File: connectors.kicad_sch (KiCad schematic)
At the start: 3 parts, among them X501 PH-00650, X502 S4B-PH-SM4-K-TB(LF)(SN), X503 USB3.1C16PFSMT

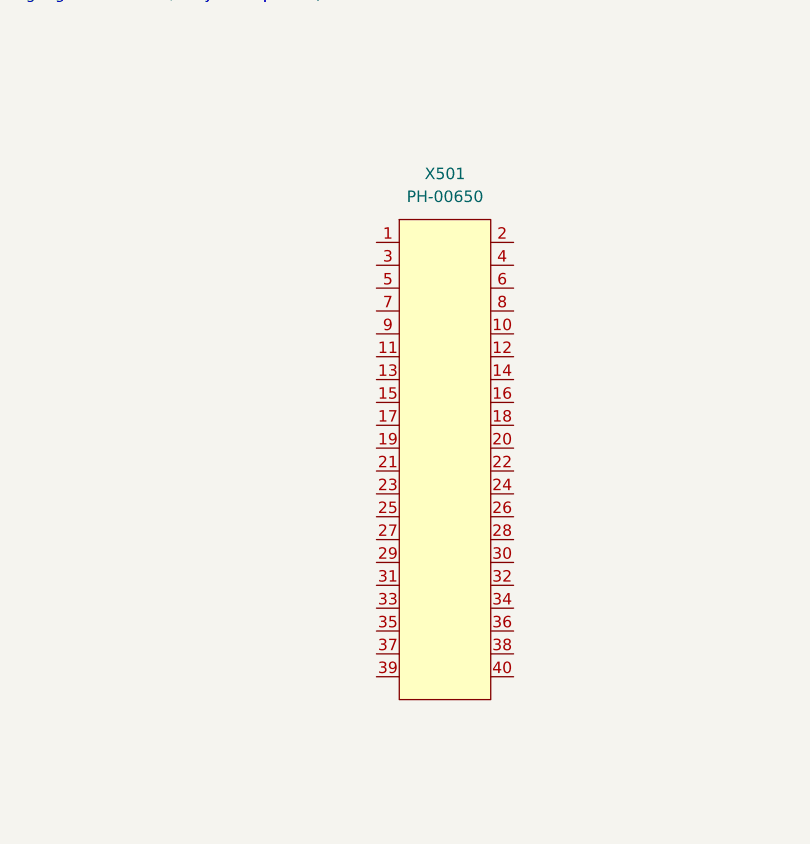
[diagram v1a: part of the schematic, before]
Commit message: Rough pcb placement for space estimation. Exchanged 40P connector
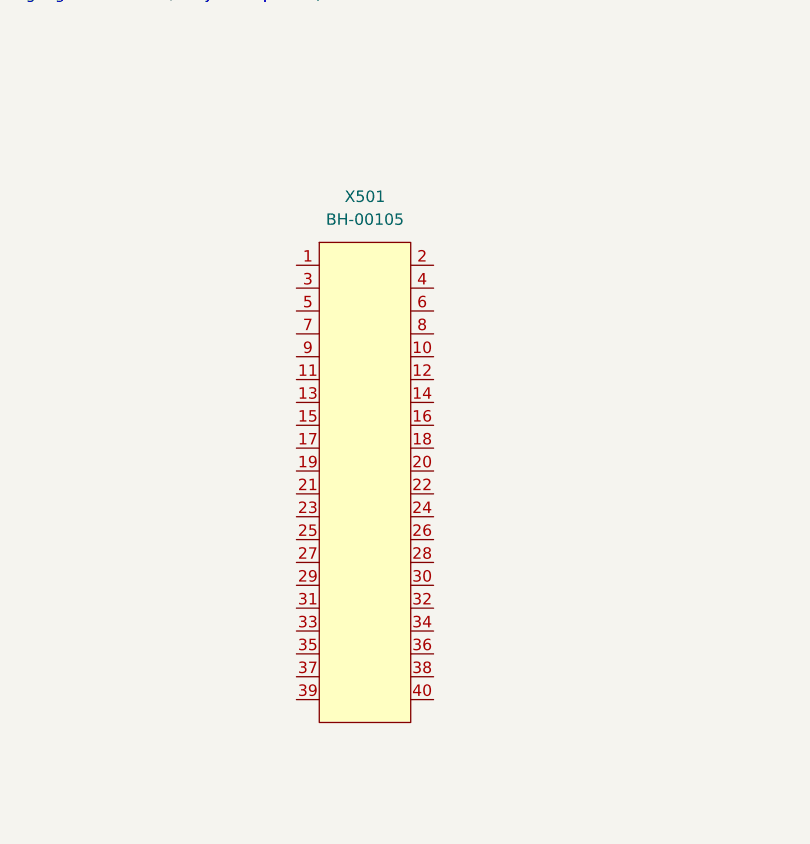
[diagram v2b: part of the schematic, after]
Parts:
- removed X501: PH-00650, HDR-SMD_40P-P2.54-V-M-R2-C20-S7.8-EH, symbol eduboardv2:PH-00650
- added X501: BH-00105, IDC-SMD_BH-00105, symbol eduboardv2:BH-00105
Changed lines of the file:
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@@
     (pin "1")
   )
-  (symbol (lib_id "eduboardv2:PH-00650") (at 78.74 81.28 0) (unit 1)
+  (symbol (lib_id "eduboardv2:GND") (at 175.26 110.49 0) (unit 1)
     (in_bom yes) (on_board yes) (fields_autoplaced)
-    (property "Reference" "X501" (id 0) (at 78.74 49.53 0))
-    (property "Value" "PH-00650" (id 1) (at 78.74 52.07 0))
-    (property "Footprint" "HDR-SMD_40P-P2.54-V-M-R2-C20-S7.8-EH" (id 2) (at 78.74 113.03 0)
+    (property "Reference" "#PWR0504" (id 0) (at 175.26 116.84 0)
       (effects (font (size 1.27 1.27)) hide)
     )
-    (property "Datasheet" "" (id 3) (at 78.74 81.28 0)
+    (property "Value" "GND" (id 1) (at 175.26 115.57 0))
+    (property "Footprint" "" (id 2) (at 175.26 110.49 0)
       (effects (font (size 1.27 1.27)) hide)
     )
-    (property "Manufacturer" "Liansheng(连盛)" (id 4) (at 78.74 118.11 0)
+    (property "Datasheet" "" (id 3) (at 175.26 110.49 0)
       (effects (font (size 1.27 1.27)) hide)
     )
-    (property "LCSC Part" "C2685175" (id 5) (at 78.74 120.65 0)
+    (pin "1")
+  )
+  (symbol (lib_id "eduboardv2:BH-00105") (at 69.85 80.01 0) (unit 1)
+    (in_bom yes) (on_board yes) (fields_autoplaced)
+    (property "Reference" "X501" (id 0) (at 69.85 52.07 0))
+    (property "Value" "BH-00105" (id 1) (at 69.85 54.61 0))
+    (property "Footprint" "IDC-SMD_BH-00105" (id 2) (at 69.85 115.57 0)
       (effects (font (size 1.27 1.27)) hide)
     )
-    (property "JLC Part" "Extended Part" (id 6) (at 78.74 123.19 0)
+    (property "Datasheet" "" (id 3) (at 69.85 80.01 0)
       (effects (font (size 1.27 1.27)) hide)
     )
-    (property "MPN" "PH-00650" (id 7) (at 78.74 110.49 0)
+    (property "Manufacturer" "Liansheng(连盛)" (id 4) (at 69.85 120.65 0)
+      (effects (font (size 1.27 1.27)) hide)
+    )
+    (property "LCSC Part" "C2685065" (id 5) (at 69.85 123.19 0)
+      (effects (font (size 1.27 1.27)) hide)
+    )
+    (property "JLC Part" "Extended Part" (id 6) (at 69.85 125.73 0)
+      (effects (font (size 1.27 1.27)) hide)
+    )
+    (property "MPN" "BH-00105" (id 7) (at 69.85 113.03 0)
       (effects (font (size 1.27 1.27)) hide)
     )
@@
     (pin "9")
   )
-  (symbol (lib_id "eduboardv2:GND") (at 175.26 110.49 0) (unit 1)
-    (in_bom yes) (on_board yes) (fields_autoplaced)
-    (property "Reference" "#PWR0504" (id 0) (at 175.26 116.84 0)
-      (effects (font (size 1.27 1.27)) hide)
-    )
-    (property "Value" "GND" (id 1) (at 175.26 115.57 0))
-    (property "Footprint" "" (id 2) (at 175.26 110.49 0)
-      (effects (font (size 1.27 1.27)) hide)
-    )
-    (property "Datasheet" "" (id 3) (at 175.26 110.49 0)
-      (effects (font (size 1.27 1.27)) hide)
-    )
-    (pin "1")
-  )
   (symbol (lib_id "eduboardv2:GND") (at 162.56 115.57 0) (unit 1)

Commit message: changed pin types and fixed 3D-positions
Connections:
- removed net GND: X503.0, X503.A1 (GND), X503.A12 (GND)
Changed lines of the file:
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@@
     (pin "1")
   )
-  (symbol (lib_id "eduboardv2:GND") (at 175.26 110.49 0) (unit 1)
+  (symbol (lib_name "GND_2") (lib_id "eduboardv2:GND") (at 175.26 110.49 0) (unit 1)
     (in_bom yes) (on_board yes) (fields_autoplaced)
     (property "Reference" "#PWR0504" (id 0) (at 175.26 116.84 0)
@@
     (pin "9")
   )
-  (symbol (lib_id "eduboardv2:GND") (at 162.56 115.57 0) (unit 1)
+  (symbol (lib_name "GND_1") (lib_id "eduboardv2:GND") (at 162.56 115.57 0) (unit 1)
     (in_bom yes) (on_board yes) (fields_autoplaced)
     (property "Reference" "#PWR0502" (id 0) (at 162.56 121.92 0)
@@
     (pin "1")
   )
-  (symbol (lib_id "eduboardv2:GND") (at 157.48 72.39 0) (unit 1)
+  (symbol (lib_name "GND_3") (lib_id "eduboardv2:GND") (at 157.48 72.39 0) (unit 1)
     (in_bom yes) (on_board yes) (fields_autoplaced)
     (property "Reference" "#PWR0501" (id 0) (at 157.48 78.74 0)

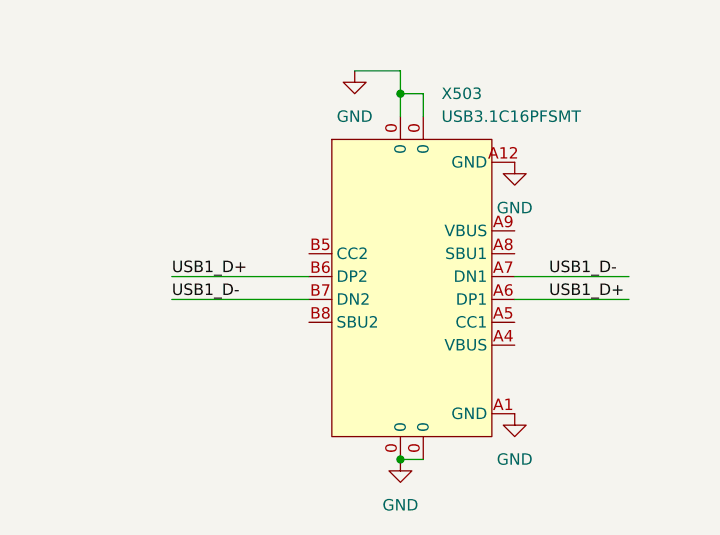
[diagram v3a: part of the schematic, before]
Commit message: change all local labels to global labels.
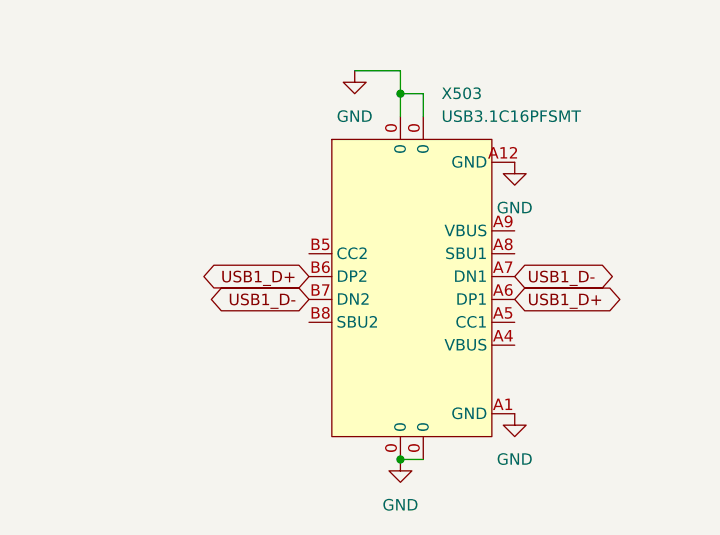
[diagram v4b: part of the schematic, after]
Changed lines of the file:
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@@
   (junction (at 162.56 74.93) (diameter 0) (color 0 0 0 0)
-  )
-  (wire (pts (xy 137.16 97.79) (xy 152.4 97.79))
-    (stroke (width 0) (type default) (color 0 0 0 0))
   )
   (wire (pts (xy 162.56 74.93) (xy 162.56 72.39))
@@
     (stroke (width 0) (type default) (color 0 0 0 0))
   )
-  (wire (pts (xy 175.26 97.79) (xy 187.96 97.79))
-    (stroke (width 0) (type default) (color 0 0 0 0))
-  )
-  (wire (pts (xy 137.16 95.25) (xy 152.4 95.25))
-    (stroke (width 0) (type default) (color 0 0 0 0))
-  )
   (wire (pts (xy 162.56 115.57) (xy 165.1 115.57))
     (stroke (width 0) (type default) (color 0 0 0 0))
@@
     (stroke (width 0) (type default) (color 0 0 0 0))
   )
-  (wire (pts (xy 175.26 95.25) (xy 187.96 95.25))
-    (stroke (width 0) (type default) (color 0 0 0 0))
-  )
   (text "Connectors\n- USB-Direct: USBC (USB)\n- RS485 Connector: ? (RS485 from Interface Chip)\n- USB-UART: USBC (USB from USB-Serial Convertor)\n- I2C: S4B-PH-SM4-K-TB(LF)(SN) + pin-header (I2C)\n- Micro-SD: TF-15x15 (SPI)\n- 40-Pin Header: PH-00650 (everything...)\n- 3.5mm Jack: (Analog Signal from DAC, maybe amplifier?)"
     (at 13.97 30.48 0)
     (effects (font (size 1.27 1.27)) (justify left bottom))
   )
-  (label "USB1_D+" (at 179.07 97.79 0)
-    (effects (font (size 1.27 1.27)) (justify left bottom))
+  (global_label "USB1_D+" (shape bidirectional) (at 175.26 97.79 0) (fields_autoplaced)
+    (effects (font (size 1.27 1.27)) (justify left))
+    (property "Intersheet References" "${INTERSHEET_REFS}" (id 0) (at 186.5026 97.8694 0)
+      (effects (font (size 1.27 1.27)) (justify left) hide)
+    )
   )
-  (label "USB1_D+" (at 137.16 95.25 0)
-    (effects (font (size 1.27 1.27)) (justify left bottom))
+  (global_label "USB1_D+" (shape bidirectional) (at 152.4 95.25 180) (fields_autoplaced)
+    (effects (font (size 1.27 1.27)) (justify right))
+    (property "Intersheet References" "${INTERSHEET_REFS}" (id 0) (at 141.1574 95.1706 0)
+      (effects (font (size 1.27 1.27)) (justify right) hide)
+    )
   )
-  (label "USB1_D-" (at 179.07 95.25 0)
-    (effects (font (size 1.27 1.27)) (justify left bottom))
+  (global_label "USB1_D-" (shape bidirectional) (at 152.4 97.79 180) (fields_autoplaced)
+    (effects (font (size 1.27 1.27)) (justify right))
+    (property "Intersheet References" "${INTERSHEET_REFS}" (id 0) (at 141.1574 97.7106 0)
+      (effects (font (size 1.27 1.27)) (justify right) hide)
+    )
   )
-  (label "USB1_D-" (at 137.16 97.79 0)
-    (effects (font (size 1.27 1.27)) (justify left bottom))
+  (global_label "USB1_D-" (shape bidirectional) (at 175.26 95.25 0) (fields_autoplaced)
+    (effects (font (size 1.27 1.27)) (justify left))
+    (property "Intersheet References" "${INTERSHEET_REFS}" (id 0) (at 186.5026 95.3294 0)
+      (effects (font (size 1.27 1.27)) (justify left) hide)
+    )
   )
   (symbol (lib_id "eduboardv2:GND") (at 175.26 82.55 0) (unit 1)

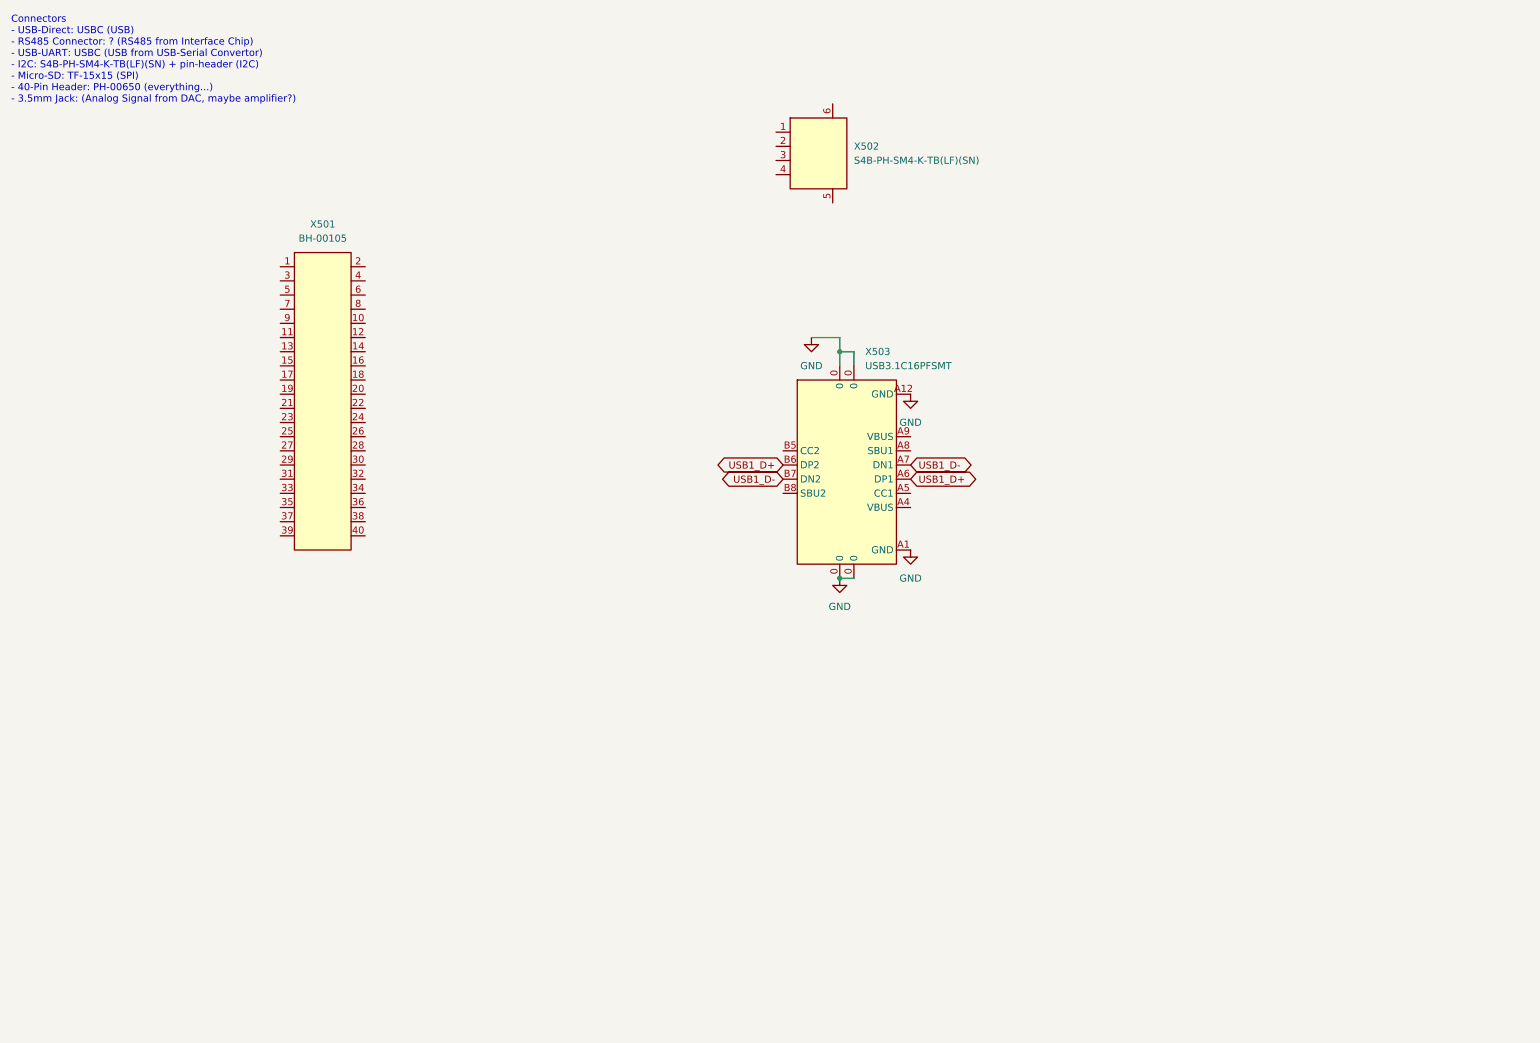
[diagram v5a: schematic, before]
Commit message: move USB Serial Converter and USB Connector to correct pages
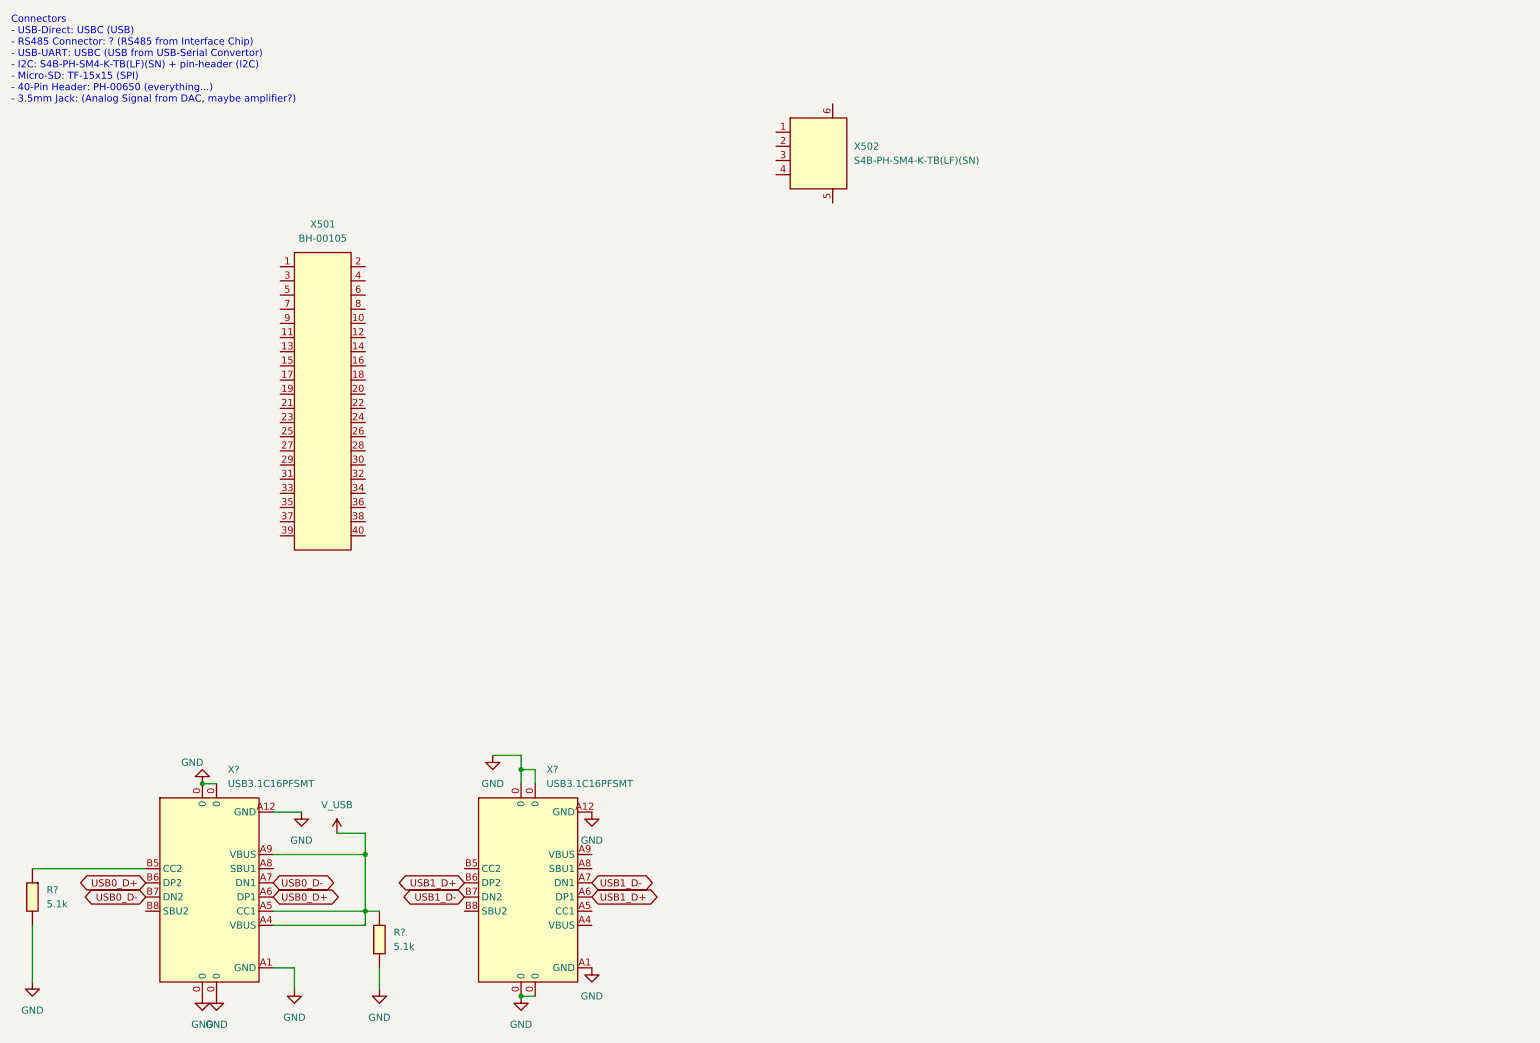
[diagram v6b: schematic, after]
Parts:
- removed X503: USB3.1C16PFSMT, USB-C-SMD_TYPE-C-USB-17, symbol eduboardv2:USB3.1C16PFSMT
- added R? (x2): 5.1k, R0402, symbol eduboardv2:0402WGF5101TCE
- added X? (x2): USB3.1C16PFSMT, USB-C-SMD_TYPE-C-USB-17, symbol eduboardv2:USB3.1C16PFSMT
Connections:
- net USB1_D+: now also X?.A6 (DP1), X?.B6 (DP2)
- net USB1_D-: now also X?.A7 (DN1), X?.B7 (DN2)
- new net: R?.2, X?.A4 (VBUS), X?.A5 (CC1), X?.A9 (VBUS)
- new net: R?.1, X?.B5 (CC2)
- new net USB0_D+: X?.A6 (DP1), X?.B6 (DP2)
- new net USB0_D-: X?.A7 (DN1), X?.B7 (DN2)
